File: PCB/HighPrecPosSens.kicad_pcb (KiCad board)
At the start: 2 copper layers, 1 part

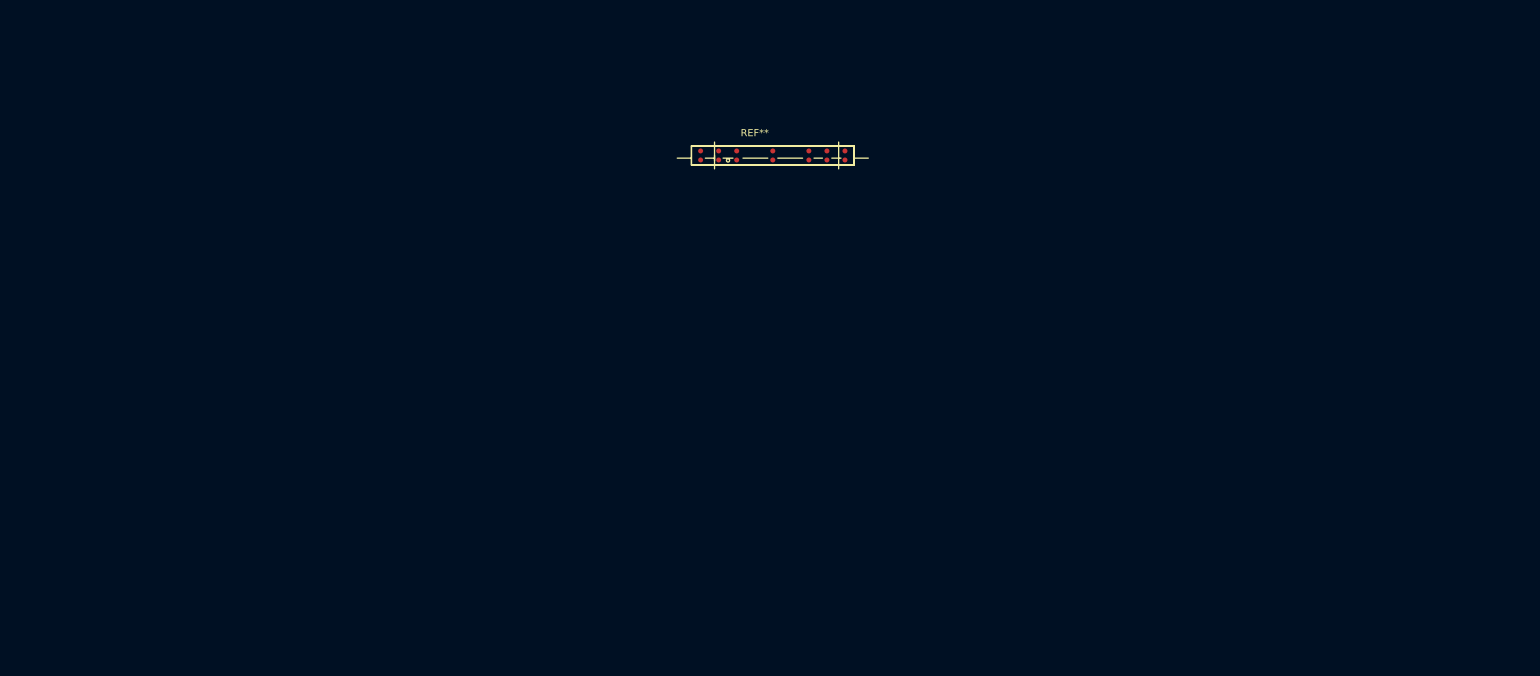
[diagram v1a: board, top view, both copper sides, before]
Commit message: First netlist transfer
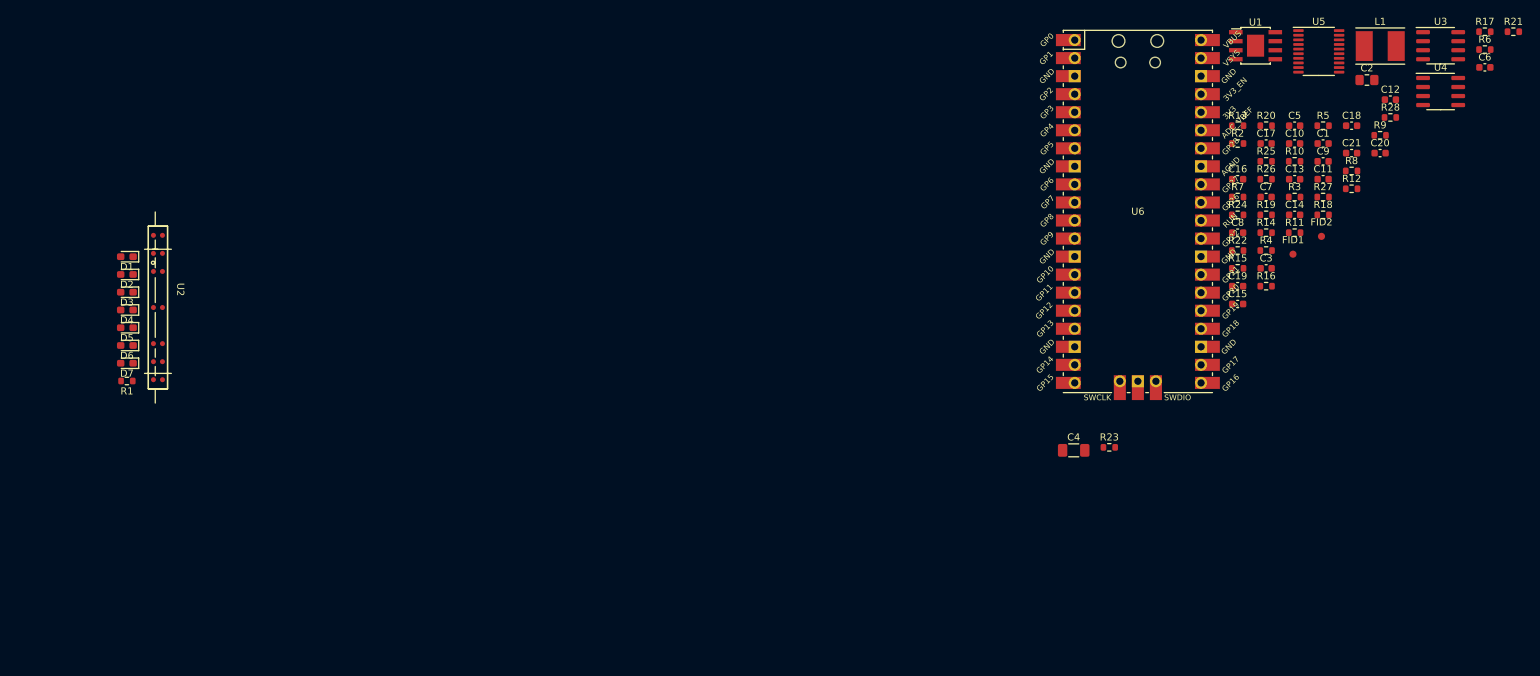
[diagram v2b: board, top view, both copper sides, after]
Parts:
- removed REF**: s12443, SensorLibrary:s12443
- added C1: 100n, Capacitor_SMD:C_0603_1608Metric, F.Cu at (203.4, 74.1)
- added C10: 100n, Capacitor_SMD:C_0603_1608Metric, F.Cu at (199.4, 74.1)
- added C11: 22u, Capacitor_SMD:C_0603_1608Metric, F.Cu at (203.4, 79.1)
- added C12: 22u, Capacitor_SMD:C_0603_1608Metric, F.Cu at (212.9, 67.9)
- added C13: 100n, Capacitor_SMD:C_0603_1608Metric, F.Cu at (199.4, 79.1)
- added C14: 100n, Capacitor_SMD:C_0603_1608Metric, F.Cu at (199.4, 84.1)
- added C15: 22u, Capacitor_SMD:C_0603_1608Metric, F.Cu at (191.4, 96.7)
- added C16: 100n, Capacitor_SMD:C_0603_1608Metric, F.Cu at (191.4, 79.1)
- added C17: 1u, Capacitor_SMD:C_0603_1608Metric, F.Cu at (195.4, 74.1)
- added C18: 1u, Capacitor_SMD:C_0603_1608Metric, F.Cu at (207.4, 71.6)
- added C19: 1u, Capacitor_SMD:C_0603_1608Metric, F.Cu at (191.4, 94.2)
- added C2: 10u, Capacitor_SMD:C_0805_2012Metric_Pad1.18x1.45mm_HandSolder, F.Cu at (209.6, 65.1)
- added C20: 1u, Capacitor_SMD:C_0603_1608Metric, F.Cu at (211.4, 75.4)
- added C21: 100n, Capacitor_SMD:C_0603_1608Metric, F.Cu at (207.4, 75.4)
- added C3: 100n, Capacitor_SMD:C_0603_1608Metric, F.Cu at (195.4, 91.6)
- added C4: 100u, Capacitor_SMD:C_1206_3216Metric_Pad1.33x1.80mm_HandSolder, F.Cu at (168.3, 117.3)
- added C5: 150p, Capacitor_SMD:C_0603_1608Metric, F.Cu at (199.4, 71.6)
- added C6: 22u, Capacitor_SMD:C_0603_1608Metric, F.Cu at (226.2, 63.4)
- added C7: 22u, Capacitor_SMD:C_0603_1608Metric, F.Cu at (195.4, 81.6)
- added C8: 1u, Capacitor_SMD:C_0603_1608Metric, F.Cu at (191.4, 86.6)
- added C9: 100n, Capacitor_SMD:C_0603_1608Metric, F.Cu at (203.4, 76.6)
- added D1: LED, LED_SMD:LED_0603_1608Metric_Pad1.05x0.95mm_HandSolder, F.Cu at (35.0, 90.0)
- added D2: LED, LED_SMD:LED_0603_1608Metric_Pad1.05x0.95mm_HandSolder, F.Cu at (35.0, 92.5)
- added D3: LED, LED_SMD:LED_0603_1608Metric_Pad1.05x0.95mm_HandSolder, F.Cu at (35.0, 95.0)
- added D4: LED, LED_SMD:LED_0603_1608Metric_Pad1.05x0.95mm_HandSolder, F.Cu at (35.0, 97.5)
- added D5: LED, LED_SMD:LED_0603_1608Metric_Pad1.05x0.95mm_HandSolder, F.Cu at (35.0, 100.0)
- added D6: LED, LED_SMD:LED_0603_1608Metric_Pad1.05x0.95mm_HandSolder, F.Cu at (35.0, 102.5)
- added D7: LED, LED_SMD:LED_0603_1608Metric_Pad1.05x0.95mm_HandSolder, F.Cu at (35.0, 105.0)
- added FID1: Fiducial, Fiducial:Fiducial_1mm_Mask2mm, F.Cu at (199.2, 89.7)
- added FID2: Fiducial, Fiducial:Fiducial_1mm_Mask2mm, F.Cu at (203.2, 87.1)
- added L1: 10u, Inductor_SMD:L_Taiyo-Yuden_NR-50xx_HandSoldering, F.Cu at (211.4, 60.4)
- added R1: 82, Resistor_SMD:R_0603_1608Metric, F.Cu at (35.0, 107.5)
- added R10: 3.6k, Resistor_SMD:R_0603_1608Metric, F.Cu at (199.4, 76.6)
- added R11: 1k, Resistor_SMD:R_0603_1608Metric, F.Cu at (199.4, 86.6)
- added R12: 1k, Resistor_SMD:R_0603_1608Metric, F.Cu at (207.4, 80.4)
- added R13: 1k, Resistor_SMD:R_0603_1608Metric, F.Cu at (191.4, 71.6)
- added R14: 4.3k, Resistor_SMD:R_0603_1608Metric, F.Cu at (195.4, 86.6)
- added R15: 82, Resistor_SMD:R_0603_1608Metric, F.Cu at (191.4, 91.6)
- added R16: 82, Resistor_SMD:R_0603_1608Metric, F.Cu at (195.4, 94.2)
- added R17: 82, Resistor_SMD:R_0603_1608Metric, F.Cu at (226.2, 58.3)
- added R18: 82, Resistor_SMD:R_0603_1608Metric, F.Cu at (203.4, 84.1)
- added R19: 82, Resistor_SMD:R_0603_1608Metric, F.Cu at (195.4, 84.1)
- added R2: 47k, Resistor_SMD:R_0603_1608Metric, F.Cu at (191.4, 74.1)
- added R20: 82, Resistor_SMD:R_0603_1608Metric, F.Cu at (195.4, 71.6)
- added R21: 1k, Resistor_SMD:R_0603_1608Metric, F.Cu at (230.2, 58.3)
- added R22: 1k, Resistor_SMD:R_0603_1608Metric, F.Cu at (191.4, 89.1)
- added R23: 1k, Resistor_SMD:R_0603_1608Metric, F.Cu at (173.3, 116.8)
- added R24: 1k, Resistor_SMD:R_0603_1608Metric, F.Cu at (191.4, 84.1)
- added R25: 82, Resistor_SMD:R_0603_1608Metric, F.Cu at (195.4, 76.6)
- added R26: 82, Resistor_SMD:R_0603_1608Metric, F.Cu at (195.4, 79.1)
- added R27: 82, Resistor_SMD:R_0603_1608Metric, F.Cu at (203.4, 81.6)
- added R28: 82, Resistor_SMD:R_0603_1608Metric, F.Cu at (212.9, 70.4)
- added R3: 4.7k, Resistor_SMD:R_0603_1608Metric, F.Cu at (199.4, 81.6)
- added R4: 2.7k, Resistor_SMD:R_0603_1608Metric, F.Cu at (195.4, 89.1)
- added R5: 82, Resistor_SMD:R_0603_1608Metric, F.Cu at (203.4, 71.6)
- added R6: 82, Resistor_SMD:R_0603_1608Metric, F.Cu at (226.2, 60.8)
- added R7: 82, Resistor_SMD:R_0603_1608Metric, F.Cu at (191.4, 81.6)
- added R8: 82, Resistor_SMD:R_0603_1608Metric, F.Cu at (207.4, 77.9)
- added R9: 100, Resistor_SMD:R_0603_1608Metric, F.Cu at (211.4, 72.9)
- added U1: ST1S14PHR, Package_SO:TI_SO-PowerPAD-8, F.Cu at (193.9, 60.3)
- added U2: S12443, SensorLibrary:s12443, F.Cu at (39.4, 97.2)
- added U3: LM393DR2G, Package_SO:SOIC-8_3.9x4.9mm_P1.27mm, F.Cu at (219.9, 60.3)
- added U4: LM393DR2G, Package_SO:SOIC-8_3.9x4.9mm_P1.27mm, F.Cu at (219.9, 66.8)
- added U5: 74LVC541A, Package_SO:TSSOP-20_4.4x6.5mm_P0.65mm, F.Cu at (202.8, 61.1)
- added U6: Pico, Pico:RPi_Pico_SMD_TH, F.Cu at (177.3, 83.6)

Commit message: Some layouting
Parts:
- moved C6 193.0 mm to (39.4, 111.8)
- moved U3 189.6 mm to (40.6, 121.9)
- moved R6 185.4 mm to (42.5, 86.4), turned to 180 degrees
- moved U4 179.5 mm to (49.1, 121.9)
- moved R17 178.8 mm to (54.6, 108.6)
- moved R9 172.3 mm to (42.5, 107.3)
- moved FID1 167.7 mm to (32.4, 72.4)
- moved C9 167.4 mm to (39.4, 109.9)
- moved R8 162.5 mm to (46.8, 102.9), turned to 180 degrees
- moved R5 161.7 mm to (42.5, 88.3)
- moved U5 160.7 mm to (46.4, 97.8)
- moved C10 160.3 mm to (39.4, 84.5)
- moved C7 156.0 mm to (39.4, 82.5)
- moved R18 149.5 mm to (54.6, 99.1)
- moved C8 148.9 mm to (42.5, 90.2)
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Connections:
- U3 pad 1: Net-(R24-Pad1) -> Net-(R21-Pad1)
- U3 pad 2: Net-(C18-Pad1) -> Net-(C17-Pad1)
- U4 pad 1: Net-(R21-Pad1) -> Net-(R24-Pad1)
- U4 pad 2: Net-(C17-Pad1) -> Net-(C18-Pad1)

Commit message: layouting
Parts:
- added D8: SS36, Diode_SMD:D_SMC_Handsoldering, F.Cu at (64.8, 128.9)
- added J1: Conn_01x02_Male, Connector_PinHeader_2.54mm:PinHeader_1x02_P2.54mm_Vertical, F.Cu at (22.5, 100.0)
- added J2: Conn_01x02_Male, Connector_PinHeader_2.54mm:PinHeader_1x02_P2.54mm_Vertical, F.Cu at (37.8, 65.9)
- added J3: Conn_01x02_Male, Connector_PinHeader_2.54mm:PinHeader_1x02_P2.54mm_Vertical, F.Cu at (22.5, 95.0)
- added J4: Conn_01x02_Male, Connector_PinHeader_2.54mm:PinHeader_1x02_P2.54mm_Vertical, F.Cu at (37.8, 70.5)
- C10, C6, C7, C9, D1, D2, D3, D4, D5, D6, D7, U2: moved to B.Cu
- moved R21 193.6 mm to (45.5, 116.3)
- moved C20 184.8 mm to (35.6, 132.1), turned to 180 degrees
- moved C18 181.0 mm to (35.6, 128.3), turned to 180 degrees
- moved R28 180.5 mm to (41.9, 128.3), turned to 180 degrees
- moved R12 175.3 mm to (38.1, 125.7), turned to 90 degrees
- moved C12 171.4 mm to (48.3, 115.6), turned to 90 degrees
- moved R10 166.5 mm to (38.1, 118.1), turned to 90 degrees
- moved C17 166.5 mm to (35.6, 120.7), turned to 180 degrees
- moved R11 165.1 mm to (38.1, 121.9), turned to 90 degrees
- moved R14 164.1 mm to (38.1, 133.3), turned to 90 degrees
- moved R13 163.9 mm to (38.1, 129.5), turned to 90 degrees
- moved C11 162.0 mm to (48.3, 125.7), turned to 90 degrees
- moved C2 158.9 mm to (68.6, 138.4), turned to -90 degrees
- moved C19 158.7 mm to (35.6, 124.5), turned to 180 degrees
- moved R26 158.3 mm to (41.9, 118.1), turned to 180 degrees
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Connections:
- net Net-(C18-Pad1) renamed /V2
- net Net-(C19-Pad1) renamed /V3
- net Net-(C20-Pad1) renamed /V1
- net Net-(R9-Pad2) renamed /V4
- R2 pad 2: Net-(R2-Pad2) -> PGood
- U1 pad 2: Net-(R2-Pad2) -> PGood
- U6 pad 20: unconnected-(U6-Pad20) -> PGood

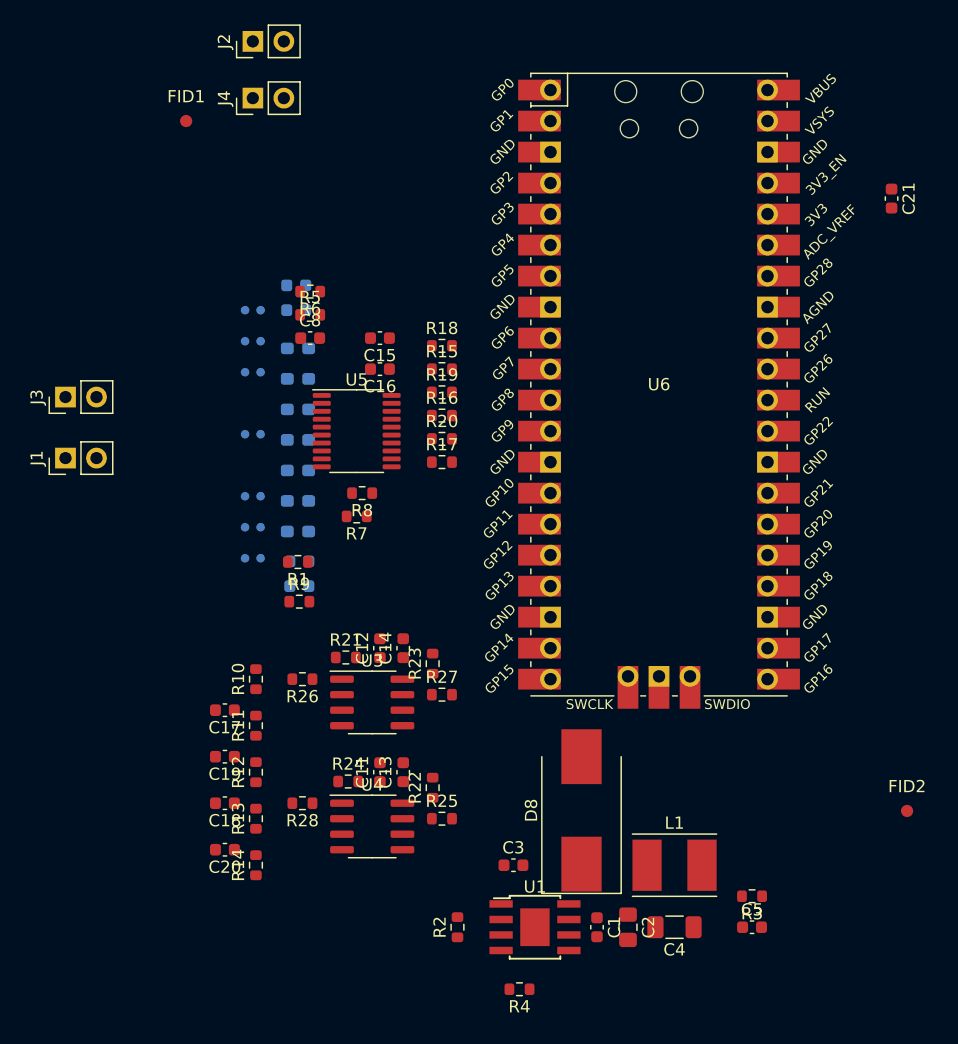
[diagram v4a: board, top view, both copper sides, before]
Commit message: Added some missing parts and more LEDs
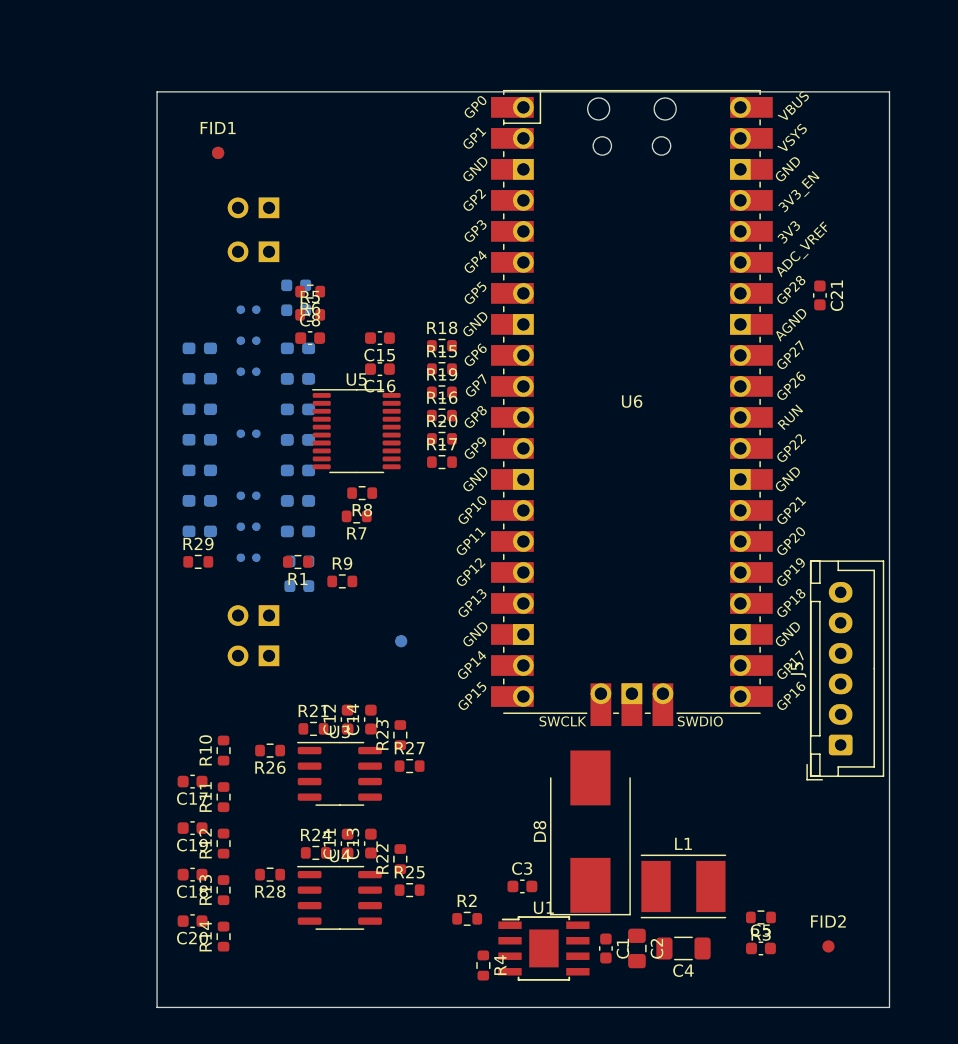
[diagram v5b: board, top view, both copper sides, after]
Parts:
- added D10: LED, LED_SMD:LED_0603_1608Metric_Pad1.05x0.95mm_HandSolder, B.Cu at (33.5, 93.5)
- added D11: LED, LED_SMD:LED_0603_1608Metric_Pad1.05x0.95mm_HandSolder, B.Cu at (33.5, 96.0)
- added D12: LED, LED_SMD:LED_0603_1608Metric_Pad1.05x0.95mm_HandSolder, B.Cu at (33.5, 98.5)
- added D13: LED, LED_SMD:LED_0603_1608Metric_Pad1.05x0.95mm_HandSolder, B.Cu at (33.5, 101.0)
- added D14: LED, LED_SMD:LED_0603_1608Metric_Pad1.05x0.95mm_HandSolder, B.Cu at (33.5, 103.5)
- added D15: LED, LED_SMD:LED_0603_1608Metric_Pad1.05x0.95mm_HandSolder, B.Cu at (33.5, 106.0)
- added D9: LED, LED_SMD:LED_0603_1608Metric_Pad1.05x0.95mm_HandSolder, B.Cu at (33.5, 91.0)
- added FID3: Fiducial, Fiducial:Fiducial_1mm_Mask2mm, B.Cu at (50.0, 115.0)
- added FID4: Fiducial, Fiducial:Fiducial_1mm_Mask2mm, B.Cu at (35.0, 75.0)
- added J5: Conn_01x06_Male, Connector_JST:JST_XH_B6B-XH-A_1x06_P2.50mm_Vertical, F.Cu at (86.0, 123.5)
- added R29: 82, Resistor_SMD:R_0603_1608Metric, F.Cu at (33.4, 108.5)
- J1, J2, J3, J4: moved to B.Cu
- moved J3 27.0 mm to (39.2, 116.2)
- moved J1 21.1 mm to (39.2, 112.9)
- moved J2 13.7 mm to (39.2, 79.5)
- moved FID2 12.8 mm to (85.0, 140.0)
- moved J4 12.7 mm to (39.2, 83.1)
- moved C21 9.87 mm to (84.3, 86.7)
- moved C19 6.42 mm to (32.9, 130.3)
- moved R27 6.42 mm to (50.7, 125.2)
- moved C11 6.42 mm to (45.6, 131.6)
- moved C12 6.42 mm to (45.6, 121.4)
- moved C13 6.42 mm to (47.5, 131.6)
- moved C14 6.42 mm to (47.5, 121.4)
- moved R12 6.42 mm to (35.5, 131.6)
- moved R21 6.42 mm to (42.8, 122.2)
- moved R24 6.42 mm to (43.0, 132.3)
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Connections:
- R20 pad 2: Net-(R20-Pad2) -> Net-(U6-Pad9)
- U6 pad 10: Net-(R20-Pad2) -> Net-(R17-Pad2)
- U6 pad 11: Net-(R17-Pad2) -> Net-(R7-Pad1)
- U6 pad 12: unconnected-(U6-Pad12) -> Net-(R8-Pad1)
- U6 pad 14: Net-(R7-Pad1) -> unconnected-(U6-Pad14)
- U6 pad 15: Net-(R8-Pad1) -> unconnected-(U6-Pad15)
- U6 pad 21: unconnected-(U6-Pad21) -> Miso
- U6 pad 22: unconnected-(U6-Pad22) -> SCS
- U6 pad 24: unconnected-(U6-Pad24) -> SCkl
- U6 pad 25: unconnected-(U6-Pad25) -> Mosi
- U6 pad 9: unconnected-(U6-Pad9) -> Net-(U6-Pad9)
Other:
- board outline added: 60 x 75 mm

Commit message: Routed layout
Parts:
- C8: moved to B.Cu
- moved C8 8.16 mm to (34.8, 87.8), turned to 90 degrees
- moved R5 4.77 mm to (42.5, 83.5), turned to 180 degrees
- moved R7 4.33 mm to (50.7, 105.0)
- moved C11 4.01 mm to (49.4, 130.1)
- moved C12 4.01 mm to (49.4, 120.0)
- moved C13 4.01 mm to (51.3, 130.1)
- moved C14 4.01 mm to (51.3, 120.0)
- moved C18 4.01 mm to (36.6, 132.7)
- moved C19 4.01 mm to (36.6, 128.8)
- moved C20 4.01 mm to (36.6, 136.5)
- moved R22 4.01 mm to (53.7, 131.4)
- moved R24 4.01 mm to (46.7, 130.9)
- moved R27 4.01 mm to (54.4, 123.8)
- moved R28 4.01 mm to (43.0, 132.7)
- moved U4 4.01 mm to (48.7, 134.6)
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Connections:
- net Net-(C3-Pad1) renamed /Boot
- net Net-(C3-Pad2) renamed /Switch
- net Net-(C5-Pad2) renamed /FB
- C17 pad 1: Net-(C17-Pad1) -> /V4
- R10 pad 1: Net-(C17-Pad1) -> /V4
- R11 pad 2: Net-(C17-Pad1) -> /V4
- R9 pad 2: /V4 -> /Video1
- U3 pad 2: Net-(C17-Pad1) -> /V4
- U3 pad 3: /V4 -> /Video1
- U3 pad 5: /V4 -> /Video1
- U4 pad 3: /V4 -> /Video1
- U4 pad 5: /V4 -> /Video1
- U6 pad 34: /V4 -> /Video1
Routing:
- net +3.3V: track 0.00 -> 237.2 mm, vias 0 -> 4
- net +24V: track 0.00 -> 136.9 mm, vias 0 -> 1
- net /Video1: track 0.00 -> 81.3 mm, vias 0 -> 3
- net GND: track 0.00 -> 76.8 mm, vias 0 -> 31
- net /D1: track 0.00 -> 43.0 mm, vias 0 -> 2
- net /D2: track 0.00 -> 39.4 mm, vias 0 -> 2
- net /D3: track 0.00 -> 34.0 mm, vias 0 -> 2
- net /D4: track 0.00 -> 30.2 mm, vias 0 -> 2
- net /FB: track 0.00 -> 30.1 mm
- net PGood: track 0.00 -> 23.2 mm, vias 0 -> 1
- net /CLk: track 0.00 -> 18.2 mm
- net /V3: track 0.00 -> 17.4 mm
- net /EOS: track 0.00 -> 16.9 mm, vias 0 -> 1
- net Net-(R18-Pad2): track 0.00 -> 16.6 mm
- net /V1: track 0.00 -> 16.5 mm
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- added copper zone on F.Cu, net +3.3V
- added copper zone on F.Cu, net /Switch
- added copper zone on B.Cu, net GND
- added copper zone on F.Cu, net GND
